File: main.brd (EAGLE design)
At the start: 49.5 x 36.8 mm, 27 parts, among them IC1 FT232RL, U1 ATMEGA328P_TQFP, Y3 16MHz

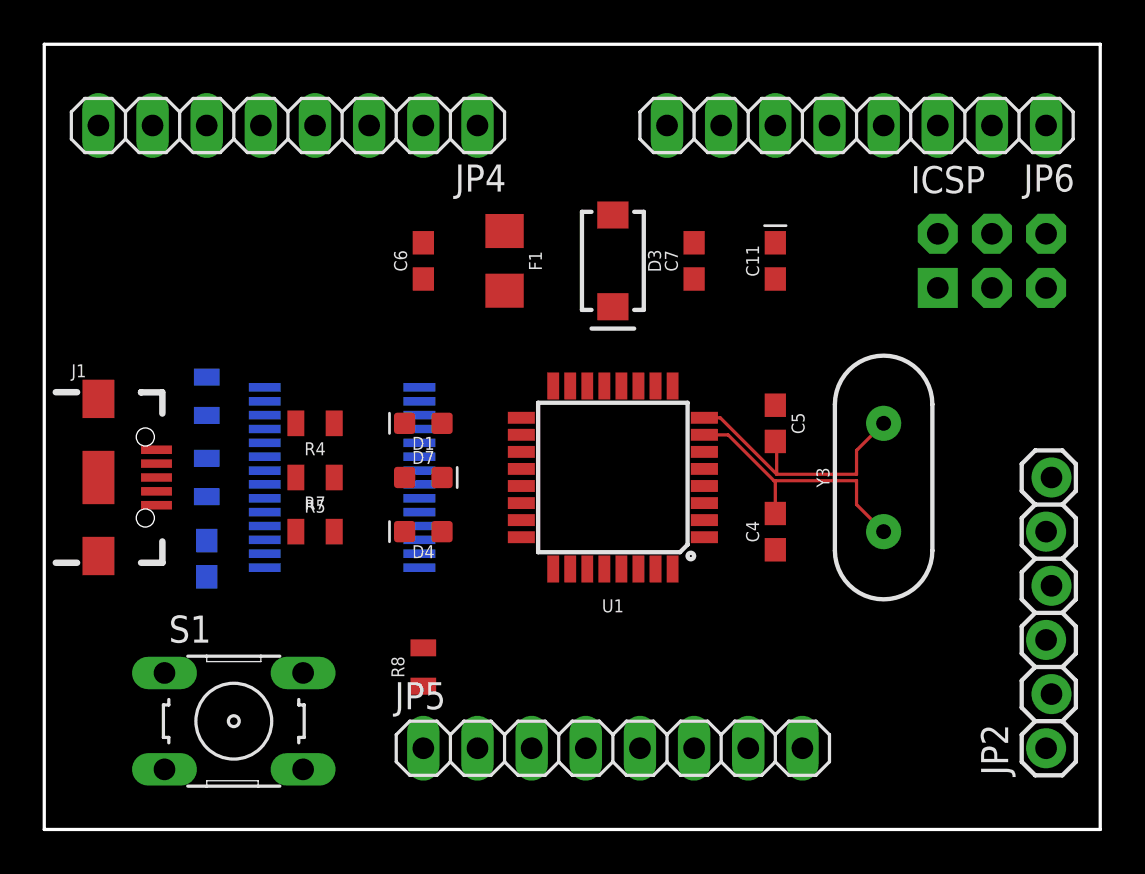
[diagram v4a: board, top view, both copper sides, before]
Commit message: ROutes RX and TX
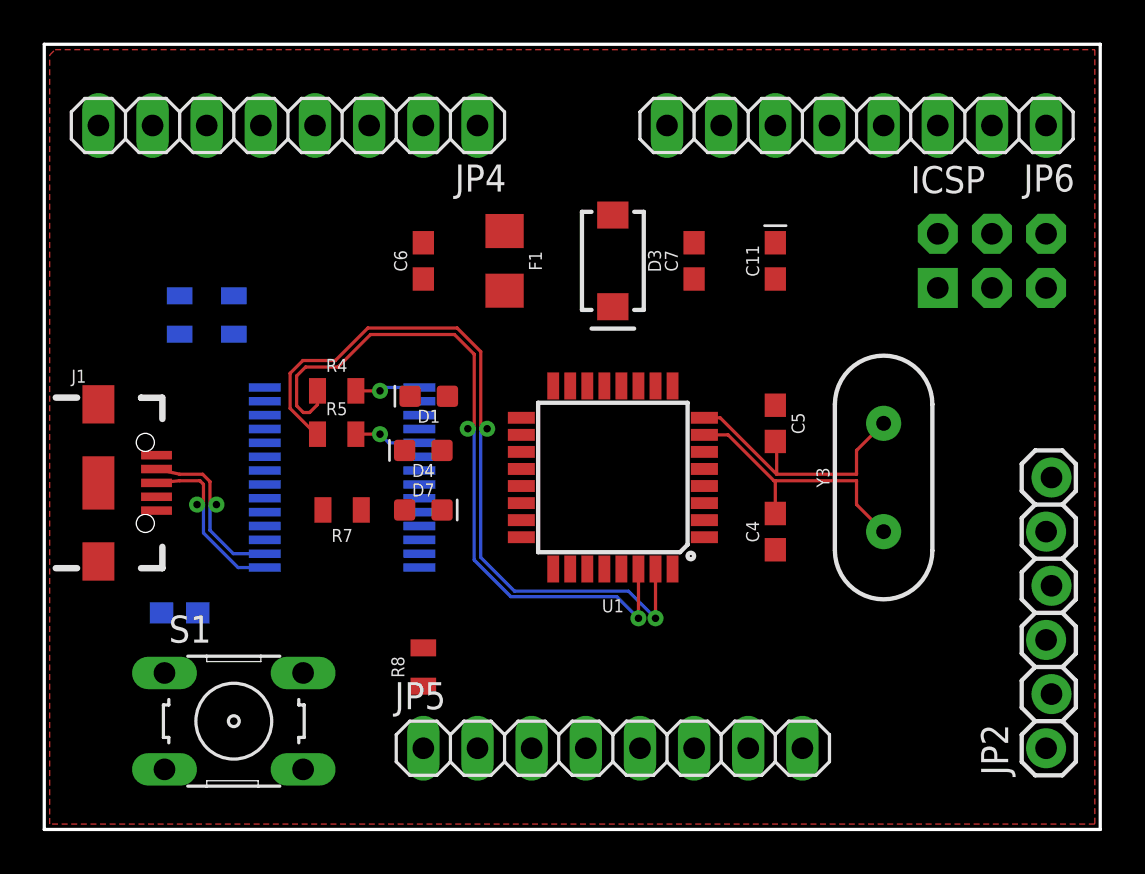
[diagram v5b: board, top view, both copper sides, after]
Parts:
- moved R2 7.73 mm to (8.89, 24.1), turned to 90 degrees
- moved R5 4.68 mm to (13.7, 18.5)
- moved R3 4.02 mm to (6.35, 24.1)
- moved D4 3.81 mm to (17.8, 17.8)
- moved C2 2.84 mm to (6.35, 10.2), turned to 180 degrees
- moved R7 1.98 mm to (14.0, 15.0)
- moved R4 1.83 mm to (13.7, 20.6), turned to 0 degrees
- moved D7 1.52 mm to (17.8, 15.0)
- moved D1 1.30 mm to (18.0, 20.3)
- moved J1 0.25 mm to (2.54, 16.3)
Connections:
- new net RX_1_N: IC1.5, R5.2
- new net RX_1_P: IC1.1, R4.2
- new net RX_N: R5.1, U1.31
- new net RX_P: R4.1, U1.30
- net RX: no longer IC1.1, IC1.5, R4.1, R4.2, R5.2, U1.30
- net TX: no longer R5.1, U1.31
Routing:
- net RX_N: track 0.00 -> 35.7 mm, vias 0 -> 2
- net RX_P: track 0.00 -> 34.2 mm, vias 0 -> 2
- net USBD_P: track 0.00 -> 8.71 mm, vias 0 -> 1
- net USBD_N: track 0.00 -> 8.59 mm, vias 0 -> 1
- net RX_1_N: track 0.00 -> 3.15 mm, vias 0 -> 1
- net RX_1_P: track 0.00 -> 3.05 mm, vias 0 -> 1
- added copper zone on layer 1, net N$1

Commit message: Autorouted
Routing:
- net GND: track 0.00 -> 105.6 mm, vias 0 -> 2
- net RST: track 0.00 -> 80.1 mm
- net RX: track 0.00 -> 60.1 mm, vias 0 -> 1
- net 5V: track 0.00 -> 56.7 mm, vias 0 -> 2
- net MOSI: track 0.00 -> 55.9 mm
- net MISO: track 0.00 -> 55.4 mm, vias 0 -> 1
- net VCC: track 0.00 -> 54.0 mm, vias 0 -> 2
- net SCK: track 0.00 -> 47.8 mm, vias 0 -> 2
- net PB2: track 0.00 -> 45.9 mm, vias 0 -> 1
- net TX: track 0.00 -> 41.3 mm, vias 0 -> 1
- net PC1: track 0.00 -> 38.3 mm, vias 0 -> 1
- net PC0: track 0.00 -> 30.8 mm, vias 0 -> 1
- net PD4: track 0.00 -> 29.0 mm
- net AREF: track 0.00 -> 26.3 mm, vias 0 -> 2
- net 3.3V: track 0.00 -> 25.1 mm, vias 0 -> 1
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- added copper zone on layer 1, net GND
- added copper zone on layer 16, net GND
- removed copper zone on layer 1, net N$1

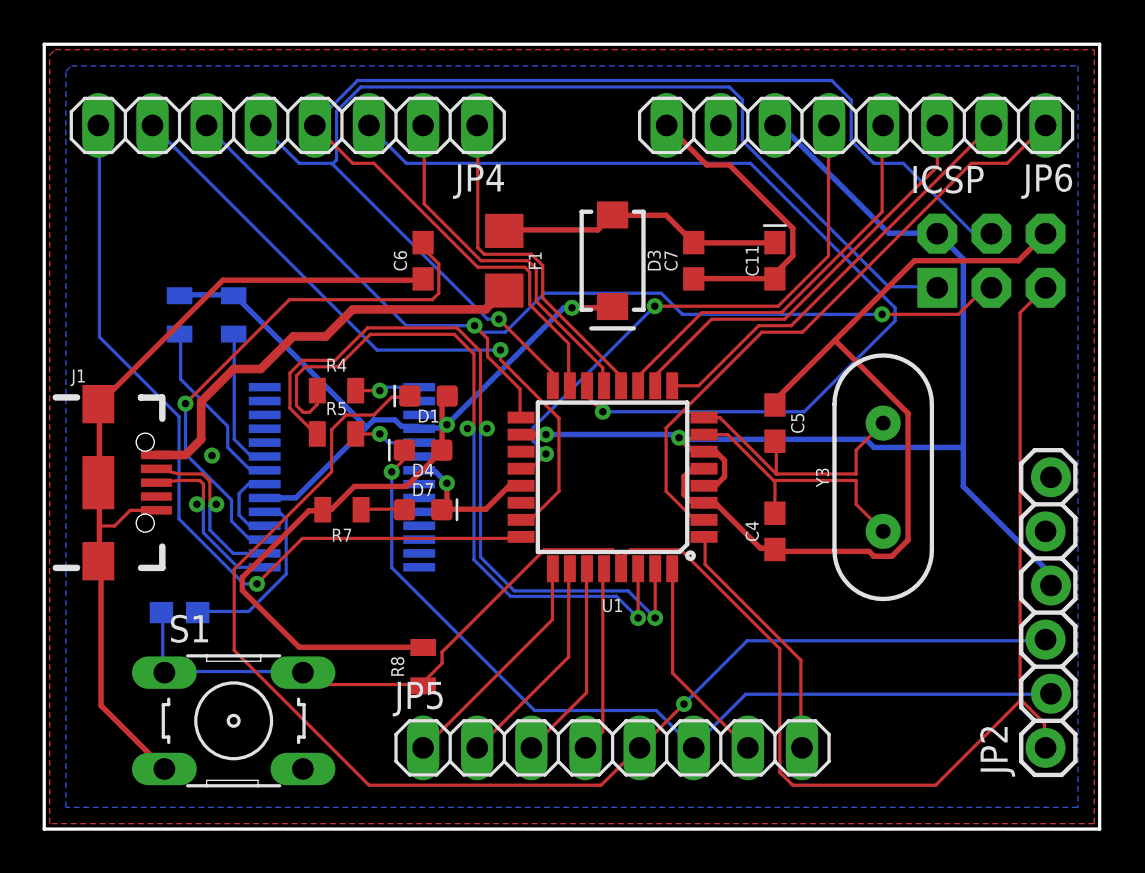
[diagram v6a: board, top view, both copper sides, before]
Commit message: Fixed DRC Errors
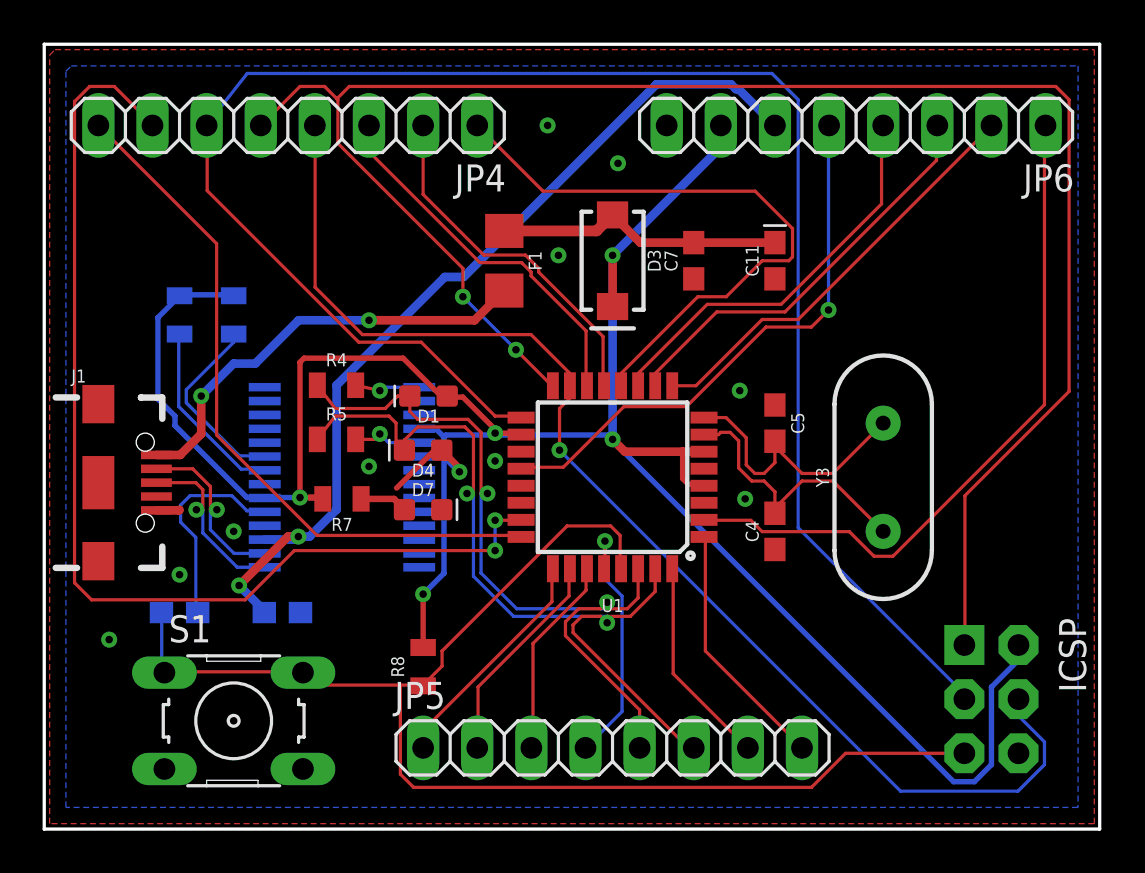
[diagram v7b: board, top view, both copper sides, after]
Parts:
- removed JP2: (no value), SparkFun-Connectors:1X06_LOCK
- moved ICSP 20.6 mm to (44.5, 6.10), turned to 270 degrees
- moved C6 17.8 mm to (11.2, 10.2), flipped to the bottom, turned to 0 degrees
- moved R7 0.51 mm to (14.0, 15.5)
- moved R5 0.25 mm to (13.7, 18.3)
- moved R4 0.25 mm to (13.7, 20.8)
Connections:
- removed net RX: D1.C, JP2.3, JP5.5
- removed net TX: D4.C, JP2.2, JP5.6
- removed net VCC: ICSP.2, JP2.4, JP6.6, U1.18, U1.4, U1.6
- net 3.3V: now also JP6.6
- net 5V: now also ICSP.2, JP6.7, U1.18, U1.4, U1.6
- net GND: no longer JP2.6
- net RST: no longer JP2.1
- net RX_N: now also D4.C, JP5.6
- net RX_P: now also D1.C, JP5.5
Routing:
- net GND: track 105.6 -> 1.10 mm, vias 2 -> 9
- net 5V: track 56.7 -> 118.7 mm, vias 2 -> 6
- net RX: track 60.1 -> 0.00 mm, vias 1 -> 0
- net VCC: track 54.0 -> 0.00 mm, vias 2 -> 0
- net TX: track 41.3 -> 0.00 mm, vias 1 -> 0
- net SCK: track 47.8 -> 83.0 mm, vias 2 -> 0
- net MISO: track 55.4 -> 84.7 mm, vias 1 -> 2
- net PB2: track 45.9 -> 17.6 mm, vias 1 -> 0
- net PC0: track 30.8 -> 51.0 mm, vias 1 -> 2
- net RST: track 80.1 -> 61.4 mm
- net 3.3V: track 25.1 -> 42.5 mm, vias 1 -> 2
- net PB0: track 16.3 -> 29.0 mm
- net PC1: track 38.3 -> 33.1 mm, vias 1 -> 0
- net PD4: track 29.0 -> 32.8 mm
- net RX_N: track 35.7 -> 39.1 mm
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
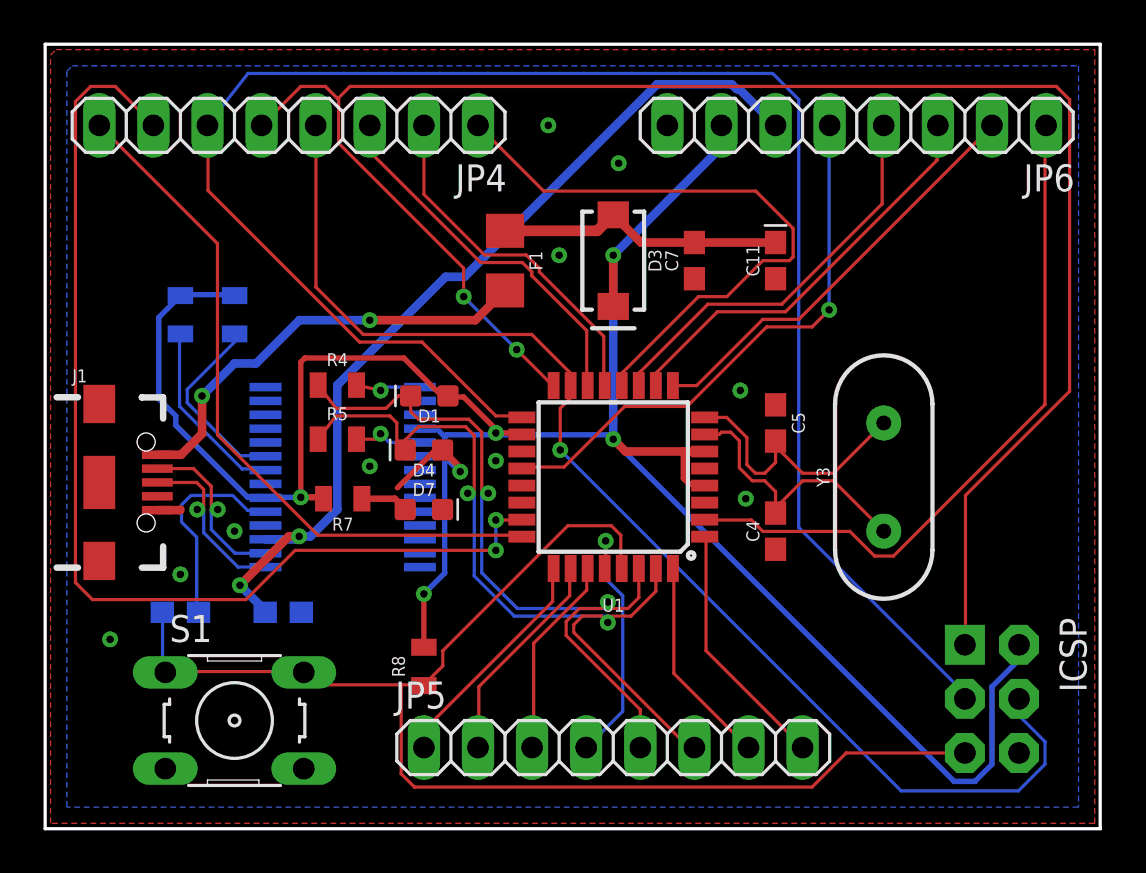
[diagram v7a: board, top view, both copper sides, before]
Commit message: Changes LED drivers to CBUS0 and CBUS1
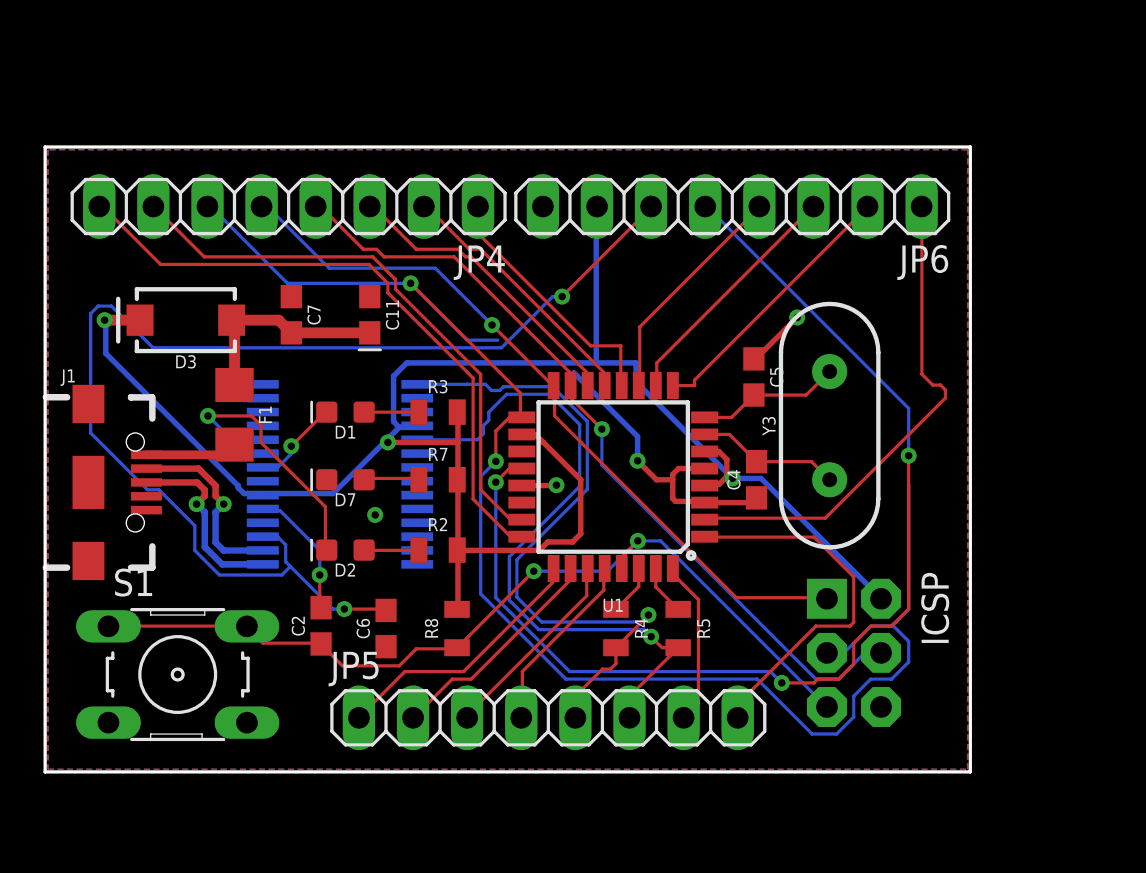
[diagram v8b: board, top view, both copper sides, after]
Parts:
- removed D4: RED, SparkFun-LED:LED-0603
- added D2: RED, SparkFun-LED:LED-0603
- moved D3 20.3 mm to (6.60, 23.9), turned to 180 degrees
- moved C11 19.2 mm to (15.2, 24.1), turned to 270 degrees
- moved C7 19.1 mm to (11.6, 24.1), turned to 270 degrees
- moved R5 18.3 mm to (29.7, 9.40), turned to 270 degrees
- moved R4 17.4 mm to (26.8, 9.40), turned to 270 degrees
- moved F1 14.6 mm to (8.89, 19.4)
- moved R2 14.6 mm to (18.4, 13.1), flipped to the top, turned to 0 degrees
- moved R3 12.9 mm to (18.4, 19.6), flipped to the top, turned to 0 degrees
- moved JP6 6.97 mm to (32.3, 29.2)
- moved ICSP 6.83 mm to (38.0, 8.26)
- moved C2 6.63 mm to (13.0, 9.53), flipped to the top, turned to 90 degrees
- moved C6 4.89 mm to (16.0, 9.40), flipped to the top, turned to 90 degrees
- moved R7 4.56 mm to (18.4, 16.4), turned to 0 degrees
- moved D1 4.01 mm to (14.1, 19.6)
- moved D7 3.94 mm to (14.1, 16.4), turned to 180 degrees
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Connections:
- new net N$1: D1.A, R3.1
- new net N$2: D2.A, R2.1
- net 5V: no longer D1.A, D4.A
- net CBUS0: now also D2.C; no longer R2.1
- net CBUS1: now also D1.C; no longer R3.1
- net RX_1_N: now also JP5.6
- net RX_1_P: now also JP5.5
- net RX_N: no longer D4.C, JP5.6
- net RX_P: no longer D1.C, JP5.5
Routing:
- net MISO: track 84.7 -> 35.0 mm, vias 2 -> 1
- net RX_N: track 39.1 -> 2.35 mm, vias 2 -> 0
- net RX_P: track 36.7 -> 2.36 mm, vias 2 -> 0
- net 5V: track 118.7 -> 88.8 mm, vias 6 -> 3
- net RX_1_P: track 3.07 -> 32.3 mm
- net RX_1_N: track 3.25 -> 32.3 mm
- net AREF: track 26.2 -> 52.9 mm, vias 1 -> 3
- net PC0: track 51.0 -> 26.8 mm, vias 2 -> 0
- net MOSI: track 58.5 -> 38.0 mm
- net RST: track 61.4 -> 41.8 mm, vias 0 -> 2
- net GND: track 1.10 -> 18.8 mm, vias 9 -> 4
- net PB0: track 29.0 -> 12.1 mm
- net VBUS: track 20.6 -> 4.33 mm, vias 2 -> 0
- net 3.3V: track 42.5 -> 56.4 mm
- net SCK: track 83.0 -> 71.5 mm, vias 0 -> 2
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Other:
- board size 49.5 x 36.8 mm -> 43.4 x 29.3 mm
